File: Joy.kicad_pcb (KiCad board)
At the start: 2 copper layers, 65 x 43 mm, 22 parts, among them IC1 MC14512BDR2G, IC2 MC14512BDR2G, J1 DB9_Male, J2 DB9_Male, J3 DB25_Male

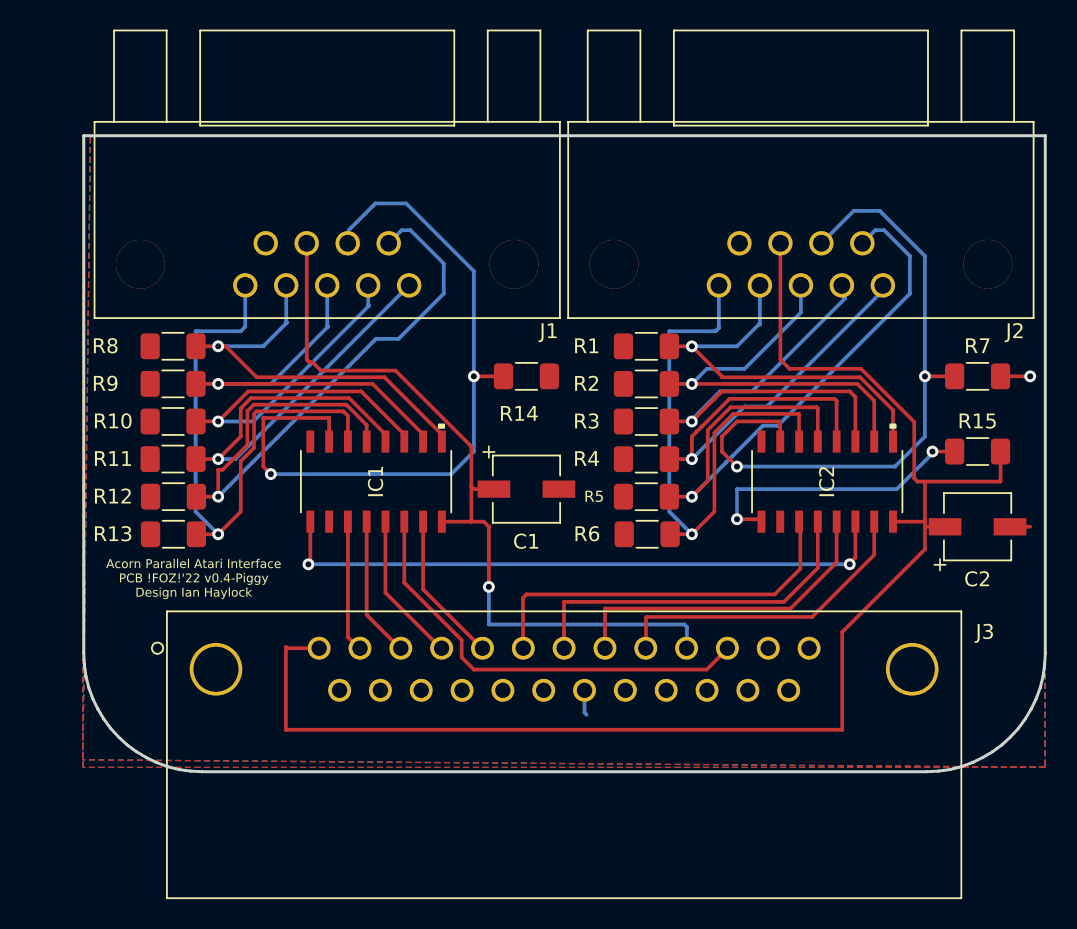
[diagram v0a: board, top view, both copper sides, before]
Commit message: Capacitors now through-hole, resistors 0805, cheaper connectors
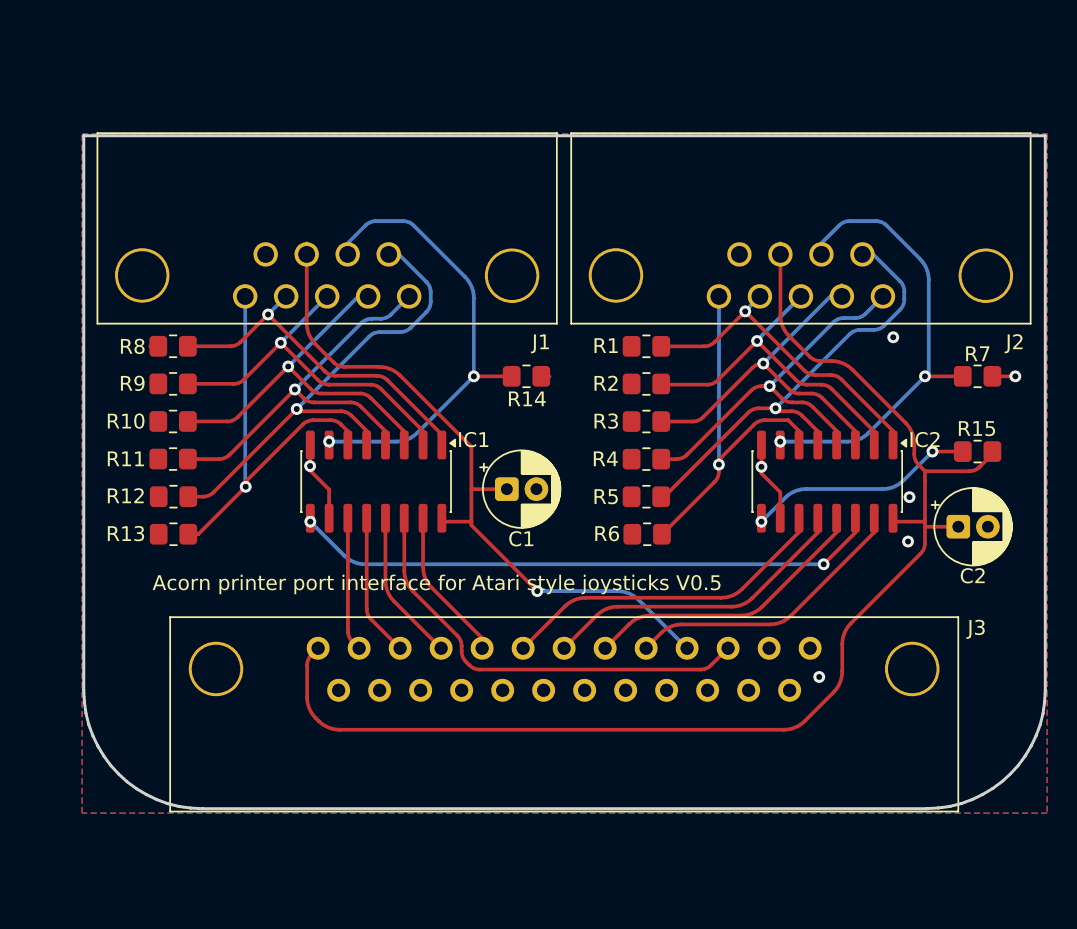
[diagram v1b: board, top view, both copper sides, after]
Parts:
- C1, C2: footprint ul_EEE-FN1A100R:EEE-FN1A100R -> Capacitor_THT:CP_Radial_D5.0mm_P2.00mm
- IC1, IC2: footprint MC14512BDR2G:MC14512BDR2G -> Package_SO:SOIC-16_3.9x9.9mm_P1.27mm
- J1, J2: footprint 5747840-6:5747840-6 -> MyFootprints:5747840-4
- J3: footprint 5747238-4:5747238-4 -> MyFootprints:5788794-1
- R1, R10, R11, R12, R13, R14, R15, R2, R3, R4, R5, R6, R7, R8, R9: footprint Resistor_SMD:R_1206_3216Metric_Pad1.30x1.75mm_HandSolder -> Resistor_SMD:R_0805_2012Metric_Pad1.20x1.40mm_HandSolder
- moved J3 16.8 mm to (86.4, 74.5)
- moved J1 8.83 mm to (70.4, 45.1)
- moved J2 8.83 mm to (102.4, 45.1)
- moved C1 1.33 mm to (82.5, 61.0)
- moved C2 1.31 mm to (113.0, 63.5)
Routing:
- net Net-(IC1-X6): track 49.7 -> 30.4 mm
- net Net-(IC2-X6): track 45.1 -> 30.5 mm
- net Net-(IC1-X4): track 46.2 -> 32.6 mm
- net Net-(IC2-X4): track 44.1 -> 30.7 mm
- net Net-(IC2-X5): track 37.7 -> 25.4 mm
- net Net-(IC1-X5): track 39.5 -> 28.0 mm
- net /Strobe: track 99.0 -> 88.4 mm
- net Net-(IC2-X3): track 34.7 -> 25.7 mm
- net Net-(IC1-X3): track 34.9 -> 27.3 mm
- net Net-(IC2-X2): track 31.4 -> 24.1 mm
- net GND: track 5.76 -> 12.9 mm, vias 1 -> 7
- net /ACK: track 53.5 -> 47.8 mm
- net Net-(IC1-X2): track 31.4 -> 25.9 mm
- net Net-(IC2-X1): track 28.3 -> 22.9 mm
- net Net-(IC2-X0): track 26.9 -> 22.0 mm
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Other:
- board size 65 x 43 mm -> 65 x 45.5 mm
- board text added: "Acorn printer port interface for Atari style joysticks V0.5"
- board text added: "Circuit by Ian Haylock, Original PCB by !FOZ!'22, some improvements by Radiofan"
- board text removed: "Acorn Parallel Atari Interface PCB !FOZ!'22 v0.4-Piggy Design Ian Haylock"
